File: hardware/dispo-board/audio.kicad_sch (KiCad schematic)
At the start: 9 parts, among them U3 CS5343, U4 CS4344

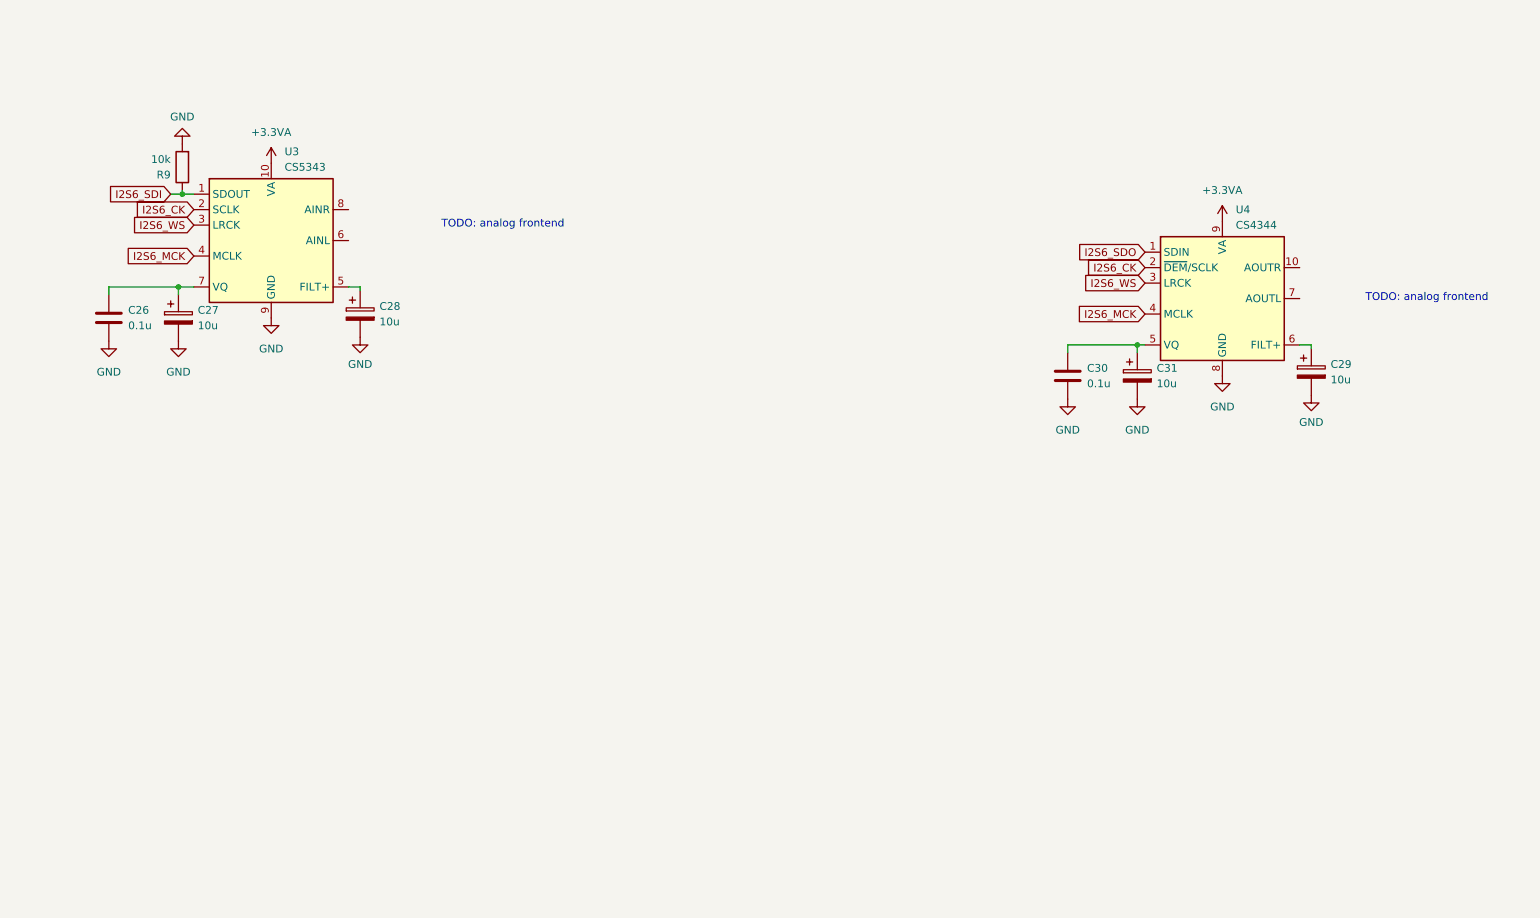
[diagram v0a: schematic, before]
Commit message: added analog frontend
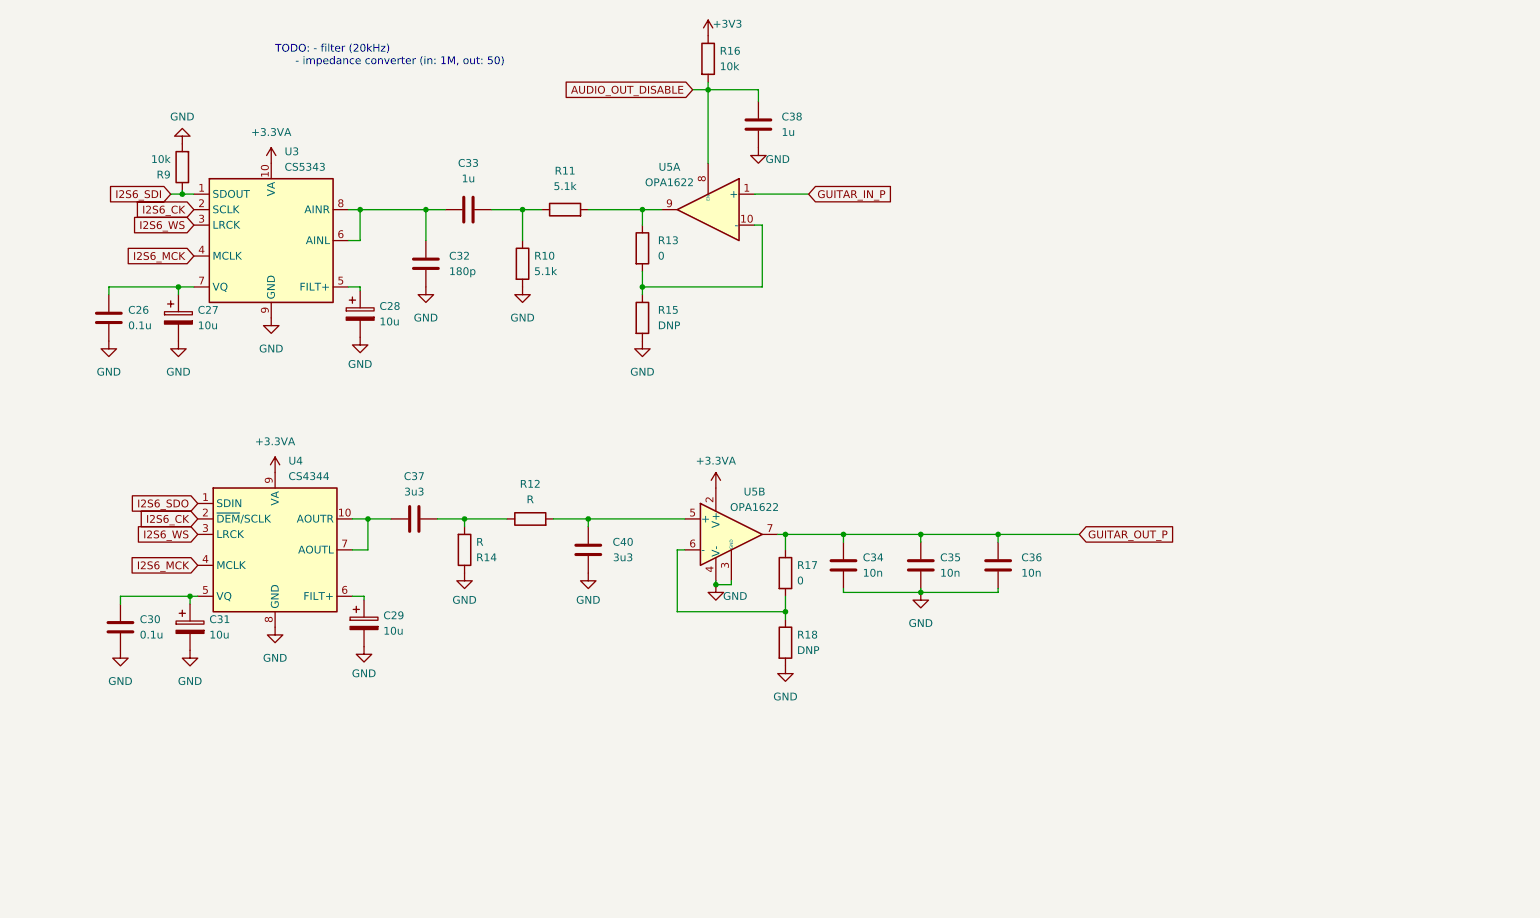
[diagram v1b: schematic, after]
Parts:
- added C32: 180p, symbol Device:C
- added C33, C38: 1u, symbol Device:C
- added C34, C35, C36: 10n, symbol Device:C
- added C37, C40: 3u3, symbol Device:C
- added R10, R11: 5.1k, symbol Device:R
- added R12, R14: R, symbol Device:R
- added R13, R17: 0, symbol Device:R
- added R15, R18: DNP, symbol Device:R
- added R16: 10k, symbol Device:R
- added U5: OPA1622, Package_SON:Texas_S-PVSON-N10, symbol Amplifier_Audio:OPA1622
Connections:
- net +3.3VA: now also U5.2 (V+)
- net GND: now also C32.2, C34.2, C35.2, C36.2, C38.2, C40.2, R10.2, R14.1, R15.2, R18.2, U5.11 (V-), U5.3 (GND), U5.4 (V-)
- net at U4.10 (AOUTR): now also U4.7 (AOUTL), C37.1
- net at U3.6 (AINL): now also U3.8 (AINR), C32.1, C33.1
- new net: R11.2, R13.1, U5.9
- new net: R13.2, R15.1, U5.10 (-)
- new net: C33.2, R10.1, R11.1
- new net: C40.1, R12.2, U5.5 (+)
- new net: R17.2, R18.1, U5.6 (-)
- new net: C37.2, R12.1, R14.2
- new net +3V3: R16.1
- new net AUDIO_OUT_DISABLE: C38.1, R16.2, U5.8 (EN)
- new net GUITAR_IN_P: U5.1 (+)
- new net GUITAR_OUT_P: C34.1, C35.1, C36.1, R17.1, U5.7
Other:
- note added: "TODO: - filter (20kHz) - impedance converter (in: 1M, out: 50)"
- note removed: "TODO: analog frontend"
- moved on the sheet: C29, C30, C31, U4

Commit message: maybe final schematic?
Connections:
- net GUITAR_IN_P renamed GUITAR_IN_µC
- net GUITAR_OUT_P renamed GUITAR_OUT_µC
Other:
- moved on the sheet: C26, C27, C28, C29, C30, C31, C32, C33, C34, C35, C36, C37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

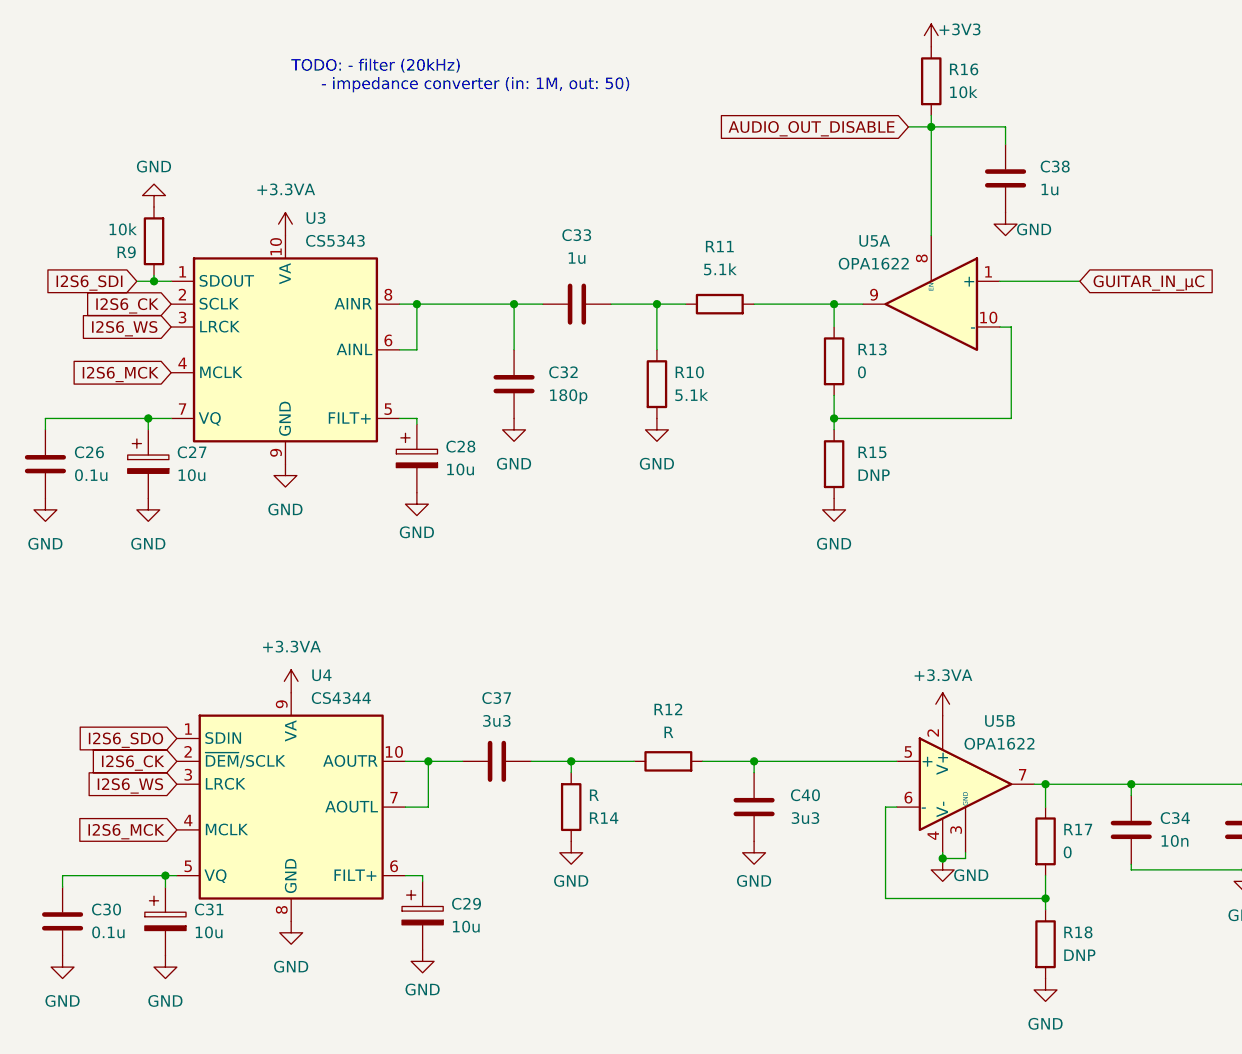
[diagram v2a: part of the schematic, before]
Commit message: added debugger, corrected erc errors
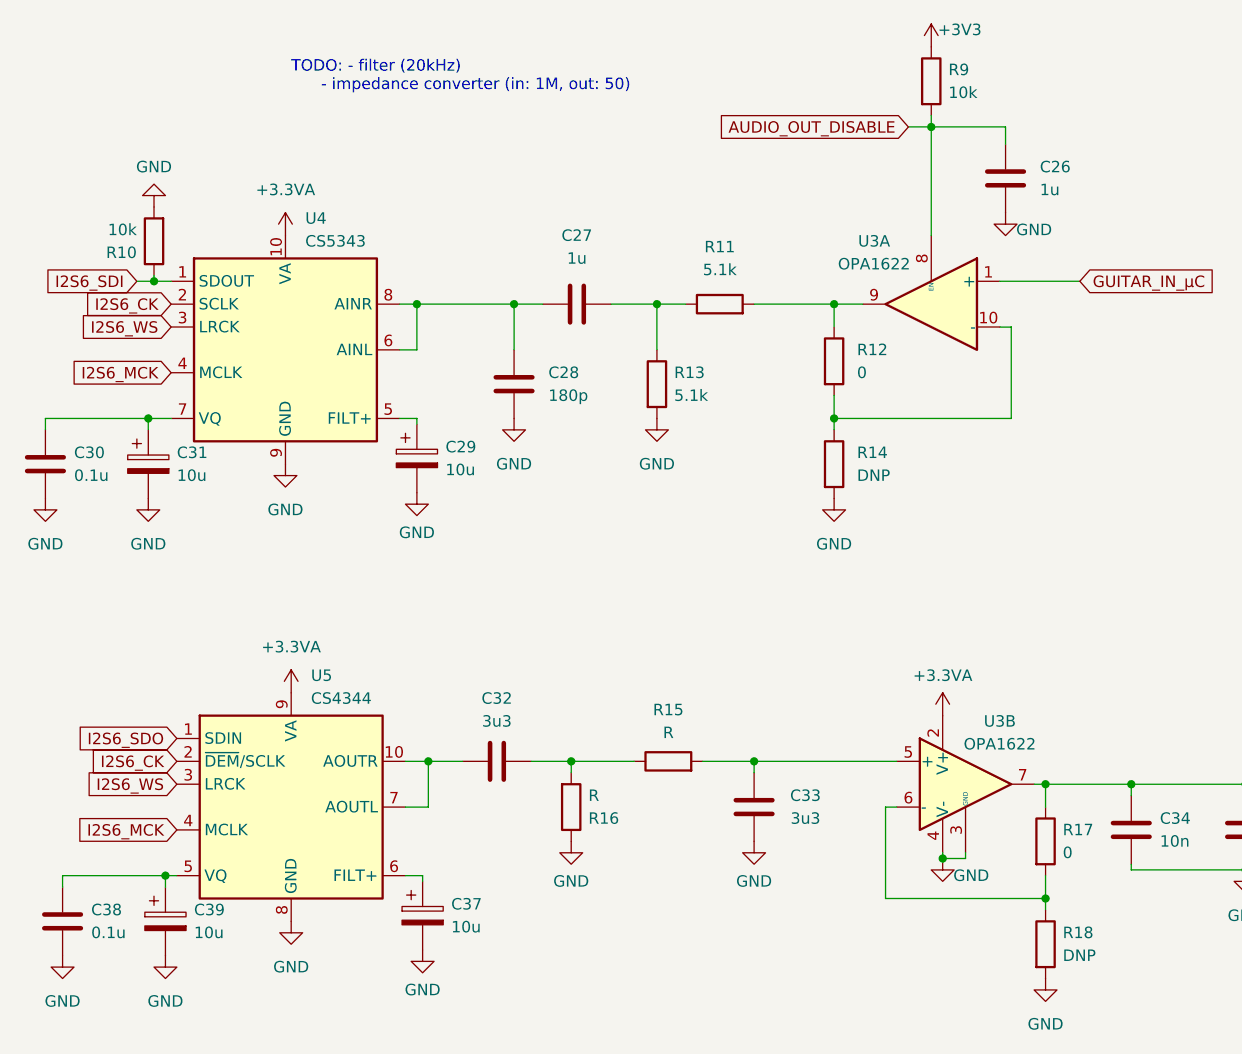
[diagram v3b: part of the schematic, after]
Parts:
- renumbered C38 to C26, C33 to C27, C32 to C28, C28 to C29, C26 to C30, C27 to C31, C37 to C32, C40 to C33, C29 to C37, C30 to C38, C31 to C39, R9 to R10, R13 to R12, R10 to R13, R15 to R14, R12 to R15, R14 to R16, R16 to R9, U5 to U3, U3 to U4, U4 to U5

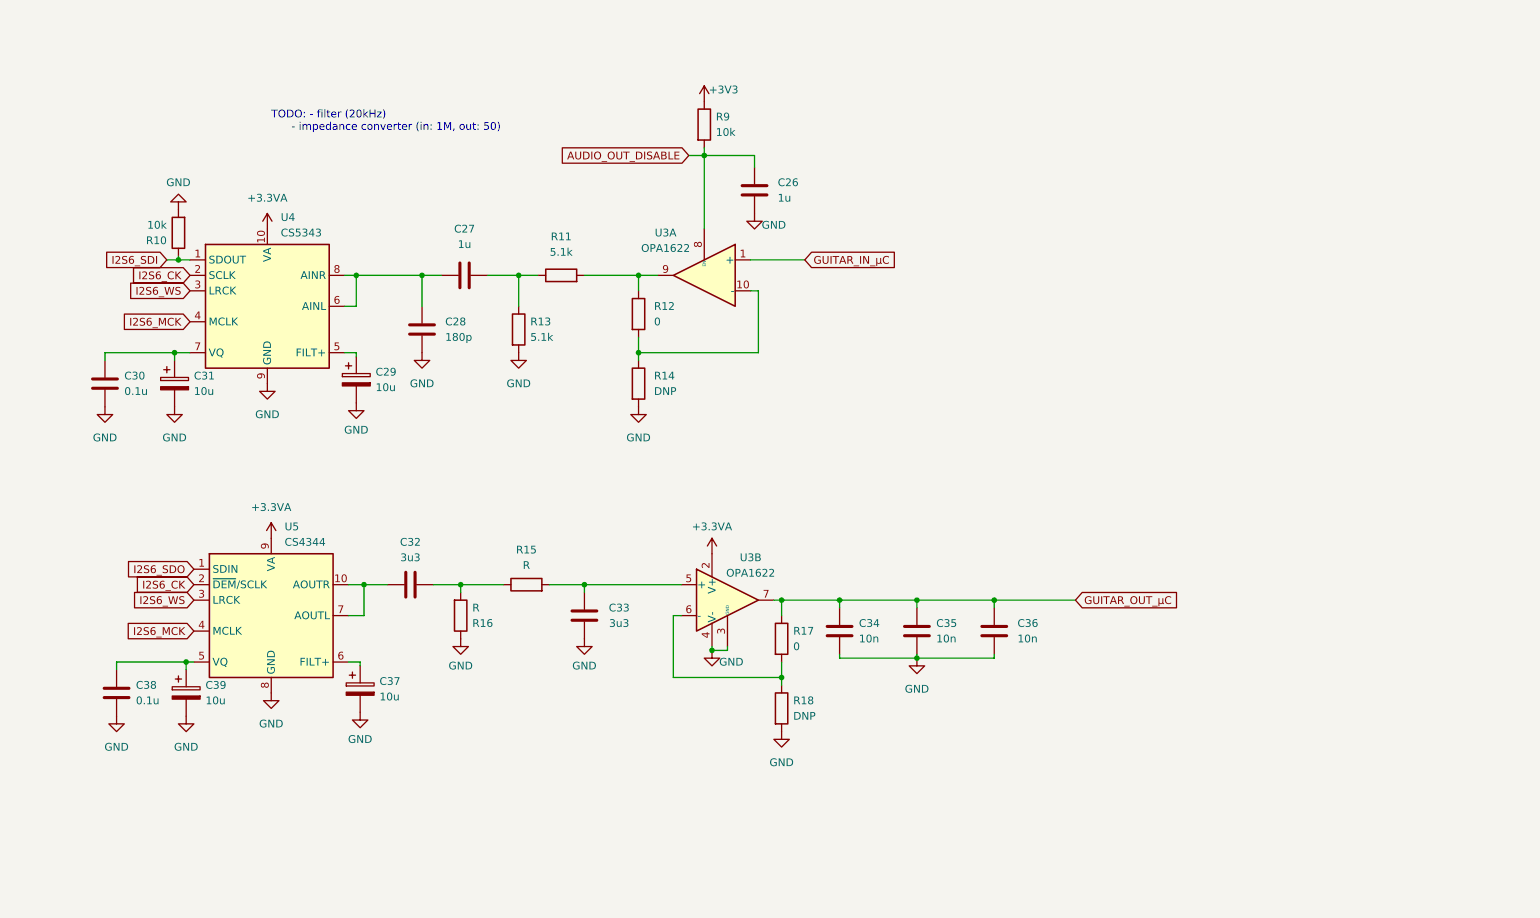
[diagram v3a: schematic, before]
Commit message: added footprints and mouser nrs
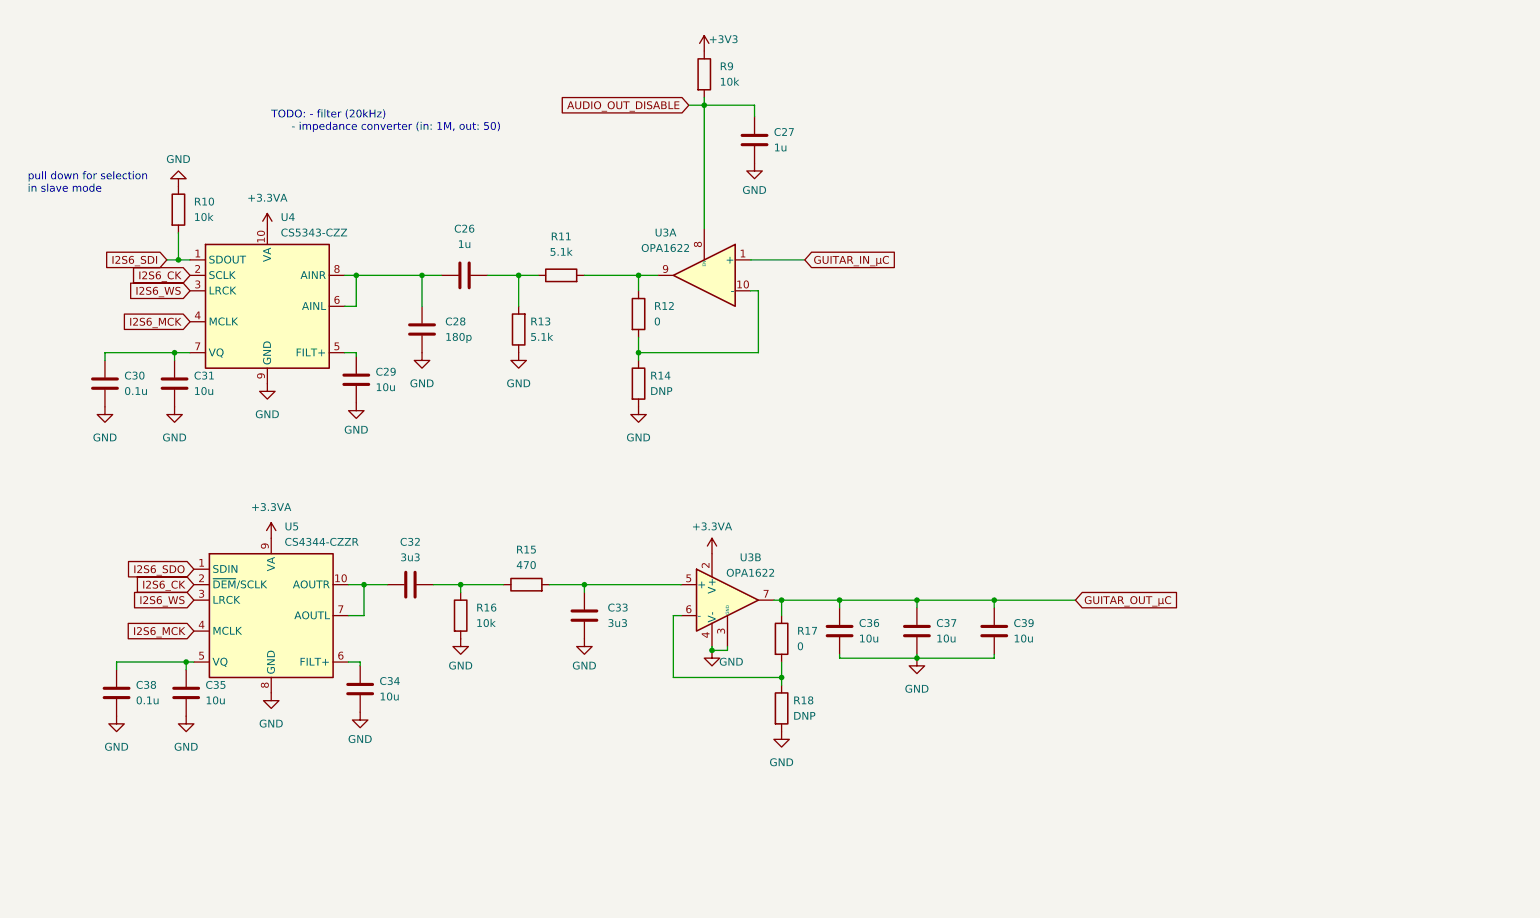
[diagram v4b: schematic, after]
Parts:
- removed C29, C31, C37, C39: 10u, symbol Device:C_Polarized
- added C29, C31, C37, C39: 10u, Capacitor_SMD:C_0603_1608Metric, symbol Device:C
- C26, C27: footprint (none) -> Capacitor_SMD:C_0603_1608Metric; MOUSER_NR (none) -> 81-GRM185R61C105KE4J
- C28: footprint (none) -> Capacitor_SMD:C_0402_1005Metric; MOUSER_NR (none) -> 81-GRM1555C1H181JA1J
- C30, C38: footprint (none) -> Capacitor_SMD:C_0402_1005Metric; MOUSER_NR (none) -> 81-GRM15R61A104KA01J
- C32, C33: footprint (none) -> Capacitor_SMD:C_0603_1608Metric; MOUSER_NR (none) -> 81-GCJ188L8EC335KE8D
- C34, C35, C36: value 10n -> 10u; footprint (none) -> Capacitor_SMD:C_0603_1608Metric; MOUSER_NR (none) -> 81-GRM188C81A106MA3D
- R10, R9: footprint (none) -> Resistor_SMD:R_0402_1005Metric; MOUSER_NR (none) -> 71-CRCW040210K0FKEDC
- R11, R13: footprint (none) -> Resistor_SMD:R_0402_1005Metric; MOUSER_NR (none) -> 71-TNPW04025K10BYEP
- R12, R17: footprint (none) -> Resistor_SMD:R_0402_1005Metric; MOUSER_NR (none) -> 710-560112110001
- R14, R18: footprint (none) -> Resistor_SMD:R_0402_1005Metric
- R15: value R -> 470; footprint (none) -> Resistor_SMD:R_0402_1005Metric; MOUSER_NR (none) -> 667-ERA-2VEB4700X
- R16: value R -> 10k; footprint (none) -> Resistor_SMD:R_0402_1005Metric; MOUSER_NR (none) -> 71-CRCW040210K0FKEDC
- U3: MOUSER_NR (none) -> 595-OPA1622IDRCR
- U4: value CS5343 -> CS5343-CZZ; MOUSER_NR (none) -> 777-CS5343-CZZ
- U5: value CS4344 -> CS4344-CZZR; MOUSER_NR (none) -> 777-CS4344-CZZR
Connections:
- net AUDIO_OUT_DISABLE: now also C27.2; no longer C26.1
- net GND: now also C27.1, C33.1, R10.1, R13.1, R16.2, C29.2, C31.2, C37.2, C39.2; no longer C26.2, C33.2, R10.2, R13.2, R16.1
- net GUITAR_OUT_µC: now also C37.1, C39.1; no longer C34.1, C35.1
- net I2S6_SDI: now also R10.2; no longer R10.1
- net at C38.1, U5.5 (VQ): now also C35.1
- net at U5.6 (FILT+): now also C34.1
- net at U4.5 (FILT+): now also C29.1
- net at C28.1, U4.6 (AINL), U4.8 (AINR): now also C26.1; no longer C27.1
- net at C30.1, U4.7 (VQ): now also C31.1
- net at R15.2, U3.5 (+): now also C33.2; no longer C33.1
- net at C32.2, R15.1: now also R16.1; no longer R16.2
- new net: C26.2, R11.1, R13.2
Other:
- note added: "pull down for selection in slave mode"
